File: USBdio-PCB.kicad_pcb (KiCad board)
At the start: 2 copper layers, 201.3 x 72.4 mm, 71 parts, among them P0 TE_RELAY_(ORWH-SH-112D), P1 TE_RELAY_(ORWH-SH-112D), P2 TE_RELAY_(ORWH-SH-112D), P3 TE_RELAY_(ORWH-SH-112D), P4 TE_RELAY_(ORWH-SH-112D), P5 TE_RELAY_(ORWH-SH-112D), P6 TE_RELAY_(ORWH-SH-112D), P7 TE_RELAY_(ORWH-SH-112D), Q1 Q_NPN_EBC, Q10 Q_NPN, Q11 Q_NPN, Q12 Q_NPN, Q13 Q_NPN, Q14 Q_NPN, Q15 Q_NPN, Q16 Q_NPN, Q17 Q_NPN, Q2 Q_NPN_EBC, Q3 Q_NPN_EBC, Q4 Q_NPN_EBC, Q5 Q_NPN_EBC, Q6 Q_NPN_EBC, Q7 Q_NPN_EBC, Q8 Q_NPN_EBC, Q9 Q_NPN_EBC, U1 Arduino_Nano

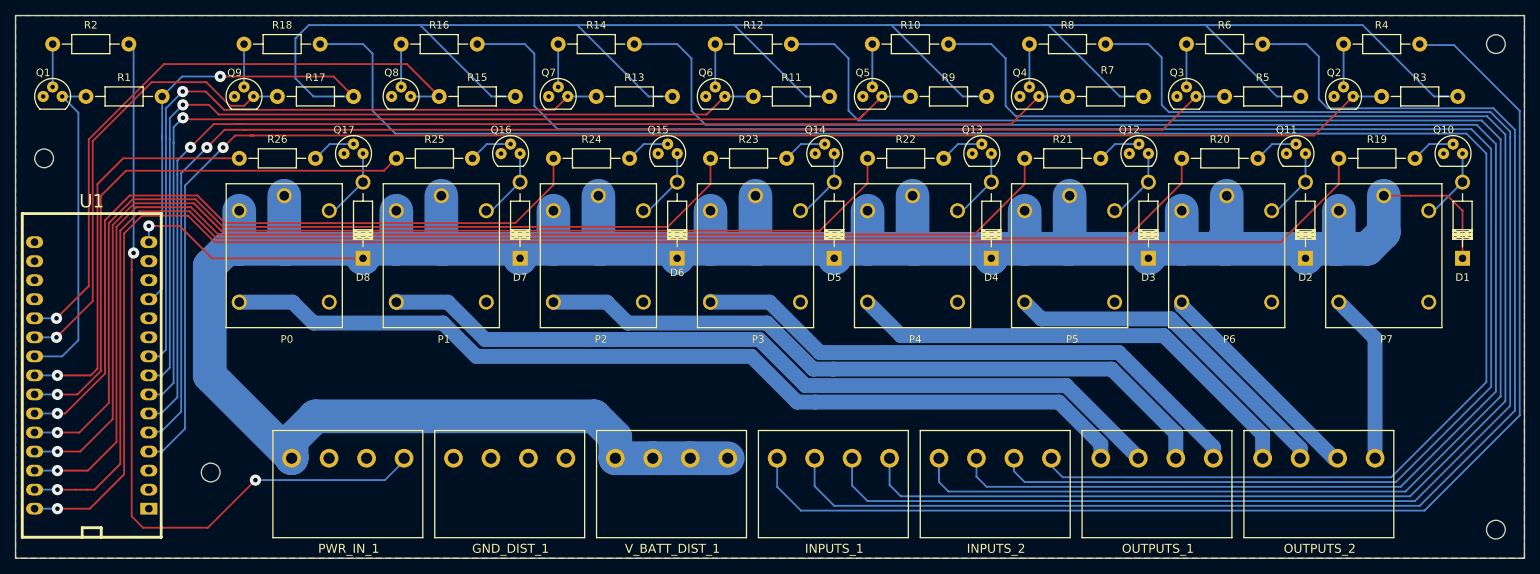
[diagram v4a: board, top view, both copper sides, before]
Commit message: changed default traces from 0.2 mm to 0.4 mm
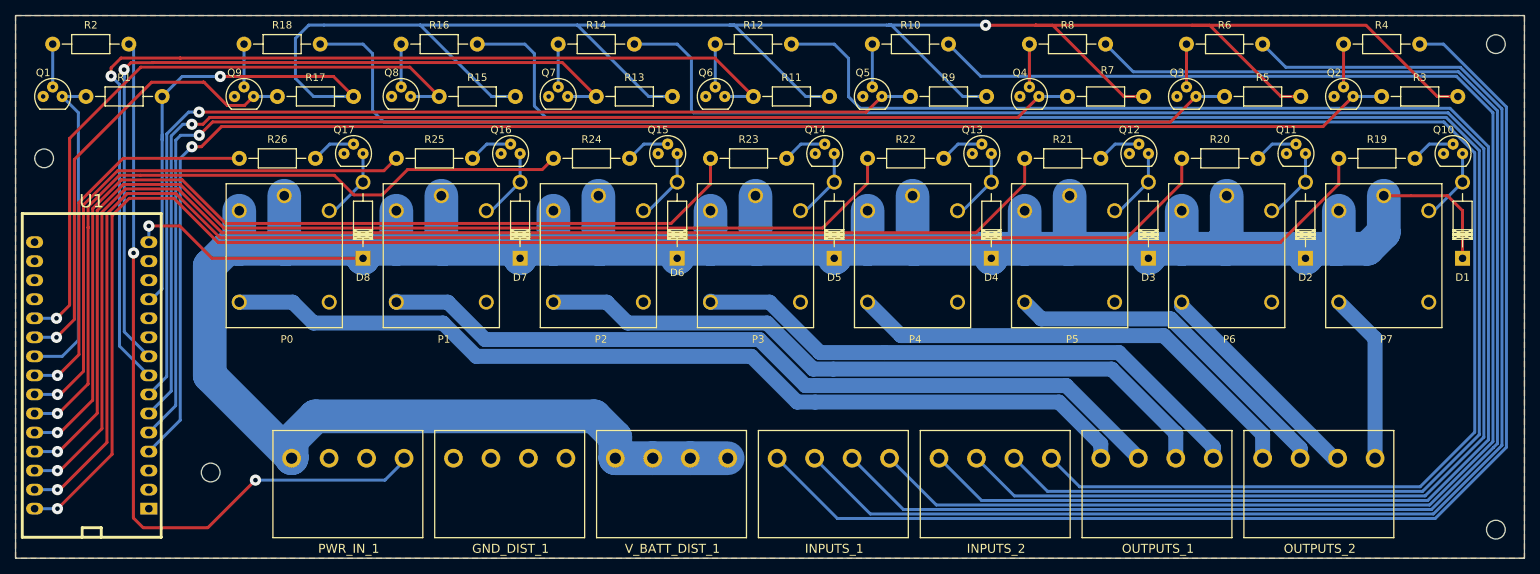
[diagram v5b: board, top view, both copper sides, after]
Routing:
- net Net-(Q6-Pad3): track 116.7 -> 135.3 mm
- net Net-(Q7-Pad3): track 94.9 -> 108.7 mm
- net Net-(INPUTS_1-Pad2): track 182.7 -> 179.0 mm
- net Net-(INPUTS_1-Pad3): track 196.7 -> 192.9 mm
- net Net-(INPUTS_1-Pad4): track 210.2 -> 206.9 mm
- net Net-(R23-Pad2): track 124.4 -> 127.1 mm
- net Net-(R26-Pad2): track 53.7 -> 51.2 mm
- net Net-(R22-Pad2): track 147.5 -> 149.9 mm
- net Net-(INPUTS_2-Pad1): track 222.1 -> 219.8 mm
- net Net-(Q5-Pad3): track 139.2 -> 137.0 mm
- net Net-(Q3-Pad3): track 181.2 -> 183.2 mm
- net Net-(R21-Pad2): track 171.2 -> 173.1 mm
- net Net-(INPUTS_1-Pad1): track 167.1 -> 165.2 mm
- net Net-(R1-Pad2): track 332.8 -> 334.6 mm, vias 1 -> 2
- net Net-(R19-Pad2): track 217.1 -> 218.9 mm
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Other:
- net class Default: trace_width 0.25 -> 0.4

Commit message: removed ground planes
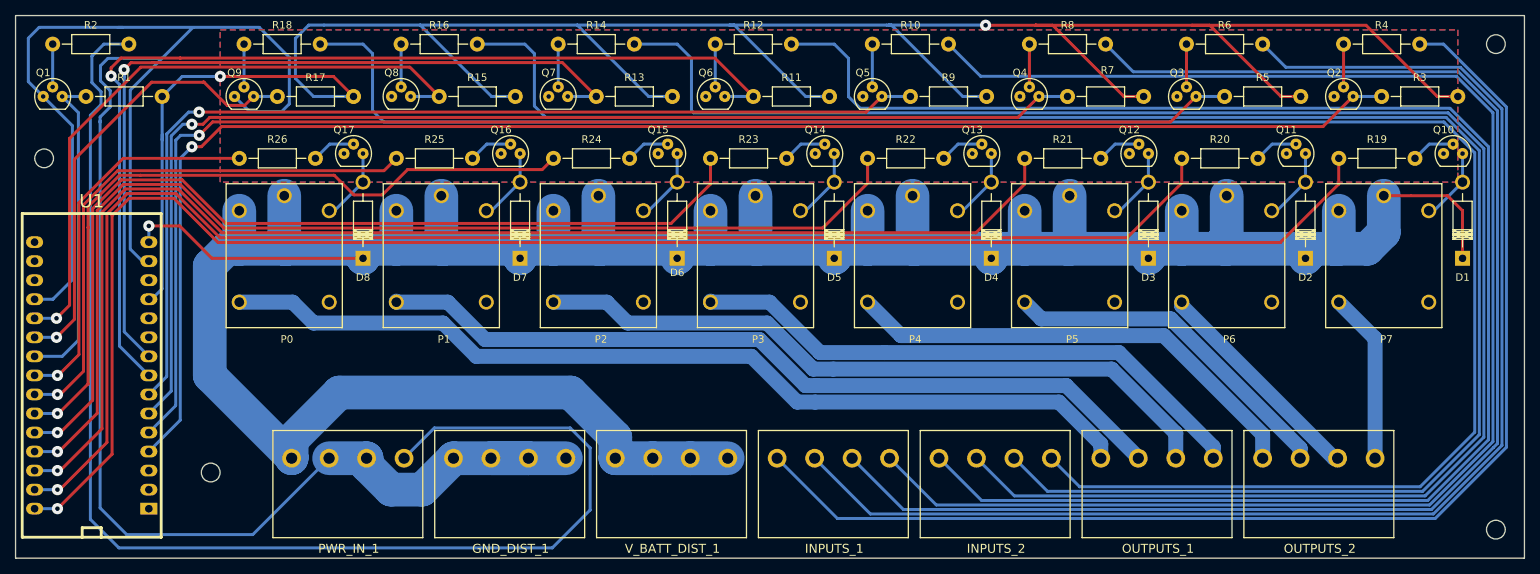
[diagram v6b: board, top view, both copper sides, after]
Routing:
- net GND: track 0.00 -> 275.9 mm
- net Net-(PWR_IN_1-Pad4): track 104.9 -> 175.1 mm, vias 2 -> 0
- net Net-(D1-Pad1): track 427.1 -> 429.7 mm

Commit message: initial commit of deutsch enclosure layout
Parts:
- removed REF** (x4): MountingHole_2.5mm, Mounting_Holes:MountingHole_2.5mm
- removed U1: Arduino_Nano, USBdio-PCB:ARDUINO_NANO
- added CONN_1: DEUTSCH_CONN_(DTM13-12PA-12PB-R008), USBdio-PCB:DEUTSCH_CONN_(DTM13-12PA-12PB-R008), F.Cu at (146.4, 137.7)
- added IC1: ATMEGA328-P, Housings_DIP:DIP-28_W7.62mm_LongPads, F.Cu at (130.1, 68.3)
- D1, D2, D3, D4, D5, D6, D7, D8: footprint Diodes_ThroughHole:Diode_DO-41_SOD81_Horizontal_RM10 -> Resistors_SMD:R_1206_HandSoldering; moved to B.Cu
- Q1, Q2, Q3, Q4, Q5, Q6, Q7, Q8, Q9: value Q_NPN_EBC -> Q_NPN_BEC; footprint USBdio-PCB:TO-92_big_pads -> TO_SOT_Packages_SMD:SOT-23_Handsoldering; moved to B.Cu
- Q10, Q11, Q12, Q13, Q14, Q15, Q16, Q17: footprint USBdio-PCB:TO-92_big_pads -> TO_SOT_Packages_SMD:SOT-23_Handsoldering; moved to B.Cu
- R1, R10, R11, R12, R13, R14, R15, R16, R17, R18, R19, R2, R20, R21, R22, R23, R24, R25, R26, R3, R4, R5, R6, R7, R8, R9: footprint Resistors_ThroughHole:Resistor_Horizontal_RM10mm -> Resistors_SMD:R_1206_HandSoldering; moved to B.Cu
- moved GND_DIST_1 144.6 mm to (105.2, 266.5)
- moved INPUTS_1 144.6 mm to (148.4, 266.5)
- moved INPUTS_2 144.6 mm to (170.0, 266.5)
- moved OUTPUTS_1 144.6 mm to (191.6, 266.5)
- moved OUTPUTS_2 144.6 mm to (213.2, 266.5)
- moved PWR_IN_1 144.6 mm to (83.6, 266.5)
- moved V_BATT_DIST_1 144.6 mm to (126.8, 266.5)
- moved R2 92.9 mm to (143.1, 80.8), turned to 270 degrees
- moved Q1 92.6 mm to (142.6, 74.3), turned to 180 degrees
- moved R1 90.4 mm to (146.1, 74.8), turned to 270 degrees
- moved R3 76.6 mm to (154.6, 53.8), turned to 90 degrees
- moved R4 68.7 mm to (157.6, 47.3), turned to 90 degrees
- moved Q2 67.1 mm to (158.1, 53.8)
- moved D1 65.3 mm to (174.1, 92.3), turned to 0 degrees
- moved R5 64.6 mm to (146.1, 53.8), turned to 90 degrees
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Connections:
- Q1 pad 1: GND -> Net-(Q1-Pad1)
- Q1 pad 2: Net-(Q1-Pad2) -> GND
- Q10 pad 1: GND -> Net-(Q10-Pad1)
- Q10 pad 2: Net-(Q10-Pad2) -> GND
- Q11 pad 1: GND -> Net-(Q11-Pad1)
- Q11 pad 2: Net-(Q11-Pad2) -> GND
- Q12 pad 1: GND -> Net-(Q12-Pad1)
- Q12 pad 2: Net-(Q12-Pad2) -> GND
- Q13 pad 1: GND -> Net-(Q13-Pad1)
- Q13 pad 2: Net-(Q13-Pad2) -> GND
- Q14 pad 1: GND -> Net-(Q14-Pad1)
- Q14 pad 2: Net-(Q14-Pad2) -> GND
- Q15 pad 1: GND -> Net-(Q15-Pad1)
- Q15 pad 2: Net-(Q15-Pad2) -> GND
- Q16 pad 1: GND -> Net-(Q16-Pad1)
- Q16 pad 2: Net-(Q16-Pad2) -> GND
- Q17 pad 1: GND -> Net-(Q17-Pad1)
- Q17 pad 2: Net-(Q17-Pad2) -> GND
- Q2 pad 1: GND -> Net-(Q2-Pad1)
- Q2 pad 2: Net-(Q2-Pad2) -> GND
- Q3 pad 1: GND -> Net-(Q3-Pad1)
- Q3 pad 2: Net-(Q3-Pad2) -> GND
- Q4 pad 1: GND -> Net-(Q4-Pad1)
- Q4 pad 2: Net-(Q4-Pad2) -> GND
- Q5 pad 1: GND -> Net-(Q5-Pad1)
- Q5 pad 2: Net-(Q5-Pad2) -> GND
- Q6 pad 1: GND -> Net-(Q6-Pad1)
- Q6 pad 2: Net-(Q6-Pad2) -> GND
- Q7 pad 1: GND -> Net-(Q7-Pad1)
- Q7 pad 2: Net-(Q7-Pad2) -> GND
- Q8 pad 1: GND -> Net-(Q8-Pad1)
- Q8 pad 2: Net-(Q8-Pad2) -> GND
- Q9 pad 1: GND -> Net-(Q9-Pad1)
- Q9 pad 2: Net-(Q9-Pad2) -> GND
- R10 pad 1: Net-(Q5-Pad2) -> Net-(Q5-Pad1)
- R12 pad 1: Net-(Q6-Pad2) -> Net-(Q6-Pad1)
- R14 pad 1: Net-(Q7-Pad2) -> Net-(Q7-Pad1)
- R16 pad 1: Net-(Q8-Pad2) -> Net-(Q8-Pad1)
- R18 pad 1: Net-(Q9-Pad2) -> Net-(Q9-Pad1)
- R19 pad 1: Net-(Q10-Pad2) -> Net-(Q10-Pad1)
- R2 pad 1: Net-(Q1-Pad2) -> Net-(Q1-Pad1)
- R20 pad 1: Net-(Q11-Pad2) -> Net-(Q11-Pad1)
- R21 pad 1: Net-(Q12-Pad2) -> Net-(Q12-Pad1)
- R22 pad 1: Net-(Q13-Pad2) -> Net-(Q13-Pad1)
- R23 pad 1: Net-(Q14-Pad2) -> Net-(Q14-Pad1)
- R24 pad 1: Net-(Q15-Pad2) -> Net-(Q15-Pad1)
- R25 pad 1: Net-(Q16-Pad2) -> Net-(Q16-Pad1)
- R26 pad 1: Net-(Q17-Pad2) -> Net-(Q17-Pad1)
- R4 pad 1: Net-(Q2-Pad2) -> Net-(Q2-Pad1)
- R6 pad 1: Net-(Q3-Pad2) -> Net-(Q3-Pad1)
- R8 pad 1: Net-(Q4-Pad2) -> Net-(Q4-Pad1)
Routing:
- net Net-(D1-Pad1): track 429.7 -> 0.00 mm, vias 1 -> 0
- net Net-(R1-Pad2): track 334.6 -> 0.00 mm, vias 2 -> 0
- net GND: track 275.9 -> 0.00 mm
- net Net-(INPUTS_2-Pad4): track 262.9 -> 0.00 mm
- net Net-(INPUTS_2-Pad3): track 248.0 -> 0.00 mm
- net Net-(INPUTS_2-Pad2): track 234.8 -> 0.00 mm
- net Net-(INPUTS_2-Pad1): track 219.8 -> 0.00 mm
- net Net-(IC1-Pad18): track 218.9 -> 0.00 mm, vias 1 -> 0
- net Net-(INPUTS_1-Pad4): track 206.9 -> 0.00 mm
- net Net-(IC1-Pad23): track 204.5 -> 0.00 mm, vias 1 -> 0
- net Net-(IC1-Pad17): track 195.7 -> 0.00 mm, vias 1 -> 0
- net Net-(INPUTS_1-Pad3): track 192.9 -> 0.00 mm
- net Net-(IC1-Pad24): track 183.2 -> 0.00 mm, vias 1 -> 0
- net Net-(INPUTS_1-Pad2): track 179.0 -> 0.00 mm
- net Net-(PWR_IN_1-Pad4): track 175.1 -> 0.00 mm
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- removed copper zone on B.Cu, net GND
- removed copper zone on F.Cu, net GND
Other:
- board size 201.3 x 72.4 mm -> 82.5 x 101.6 mm

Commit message: all footprints added.  ready for traces.
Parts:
- removed GND_DIST_1, INPUTS_1, INPUTS_2, OUTPUTS_1, OUTPUTS_2, PWR_IN_1, V_BATT_DIST_1: CONN_01X04, USBdio-PCB:PHX_HDR_4_POS_(1933202)
- added D9: D_Schottky, USBdio-PCB:SCHOTTKY_(PMEG3030EP,115), B.Cu at (177.6, 65.8)
- added P8: CONN_01X03, Pin_Headers:Pin_Header_Straight_1x03, F.Cu at (159.1, 134.8)
- added R27: 1M, Resistors_SMD:R_1206_HandSoldering, B.Cu at (153.6, 77.3)
- added R28: 10k, Resistors_SMD:R_1206_HandSoldering, B.Cu at (119.1, 68.3)
- added U1: NCV7805BDTRKG, USBdio-PCB:REGULATOR_(NCV7805BDTRKG), B.Cu at (175.1, 56.8)
- added X1: CRYSTAL_SMD, USBdio-PCB:RESONATOR_(CSTCE16M0V53C-R0), B.Cu at (152.1, 72.8)
- P0, P1, P2, P3, P4, P5, P6, P7: value TE_RELAY_(ORWH-SH-112D) -> RELAY_(JSM1A-12V-4); footprint USBdio-PCB:TE_RELAY_(ORWH-SH-112D) -> USBdio-PCB:RELAY_(JSM1A-12V-4)
- R19, R20, R21, R22, R23, R24, R25, R26: value 1k -> 680
- moved P0 2.70 mm to (116.4, 112.0)
- moved P1 2.70 mm to (132.4, 112.0)
- moved P2 2.70 mm to (148.4, 112.0)
- moved P3 2.70 mm to (164.4, 112.0)
- moved D5 2.50 mm to (174.1, 114.8)
- moved D6 2.50 mm to (158.1, 114.8)
- moved D7 2.50 mm to (142.1, 114.8)
- moved D8 2.50 mm to (126.1, 114.8)
- moved Q14 2.50 mm to (176.1, 119.3)
- moved Q15 2.50 mm to (160.1, 119.3)
- moved Q16 2.50 mm to (144.1, 119.3)
- moved Q17 2.50 mm to (128.1, 119.3)
- moved R23 2.50 mm to (180.1, 118.8)
- moved R24 2.50 mm to (164.1, 118.8)
- moved R25 2.50 mm to (148.1, 118.8)
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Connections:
- CONN_1 pad A10: Net-(CONN_1-PadA10) -> RLY1
- CONN_1 pad A11: Net-(CONN_1-PadA11) -> RLY2
- CONN_1 pad A12: Net-(CONN_1-PadA12) -> RLY3
- CONN_1 pad A2: Net-(CONN_1-PadA2) -> GND
- CONN_1 pad A3: Net-(CONN_1-PadA3) -> GND
- CONN_1 pad A9: Net-(CONN_1-PadA9) -> RLY0
- CONN_1 pad B1: Net-(CONN_1-PadB1) -> Net-(CONN_1-PadA1)
- CONN_1 pad B10: Net-(CONN_1-PadB10) -> RLY5
- CONN_1 pad B11: Net-(CONN_1-PadB11) -> RLY6
- CONN_1 pad B12: Net-(CONN_1-PadB12) -> RLY7
- CONN_1 pad B2: Net-(CONN_1-PadB2) -> Net-(CONN_1-PadA1)
- CONN_1 pad B3: Net-(CONN_1-PadB3) -> GND
- CONN_1 pad B4: Net-(CONN_1-PadB4) -> GND
- CONN_1 pad B9: Net-(CONN_1-PadB9) -> RLY4
- IC1 pad 20: Net-(IC1-Pad20) -> +5V
- IC1 pad 7: Net-(IC1-Pad7) -> +5V
- P0 pad 1: Net-(D1-Pad1) -> Net-(CONN_1-PadA1)
- P0 pad 2: Net-(D8-Pad2) -> Net-(D1-Pad1)
- P0 pad 3: Net-(D1-Pad1) -> RLY0
- P0 pad 5: Net-(P0-Pad5) -> Net-(D8-Pad2)
- P1 pad 1: Net-(D1-Pad1) -> Net-(CONN_1-PadA1)
- P1 pad 2: Net-(D7-Pad2) -> Net-(D1-Pad1)
- P1 pad 3: Net-(D1-Pad1) -> RLY1
- P1 pad 5: Net-(P1-Pad5) -> Net-(D7-Pad2)
- P2 pad 1: Net-(D1-Pad1) -> Net-(CONN_1-PadA1)
- P2 pad 2: Net-(D6-Pad2) -> Net-(D1-Pad1)
- P2 pad 3: Net-(D1-Pad1) -> RLY2
- P2 pad 5: Net-(P2-Pad5) -> Net-(D6-Pad2)
- P3 pad 1: Net-(D1-Pad1) -> Net-(CONN_1-PadA1)
- P3 pad 2: Net-(D5-Pad2) -> Net-(D1-Pad1)
- P3 pad 3: Net-(D1-Pad1) -> RLY3
- P3 pad 5: Net-(P3-Pad5) -> Net-(D5-Pad2)
- P4 pad 1: Net-(D1-Pad1) -> Net-(CONN_1-PadA1)
- P4 pad 2: Net-(D4-Pad2) -> Net-(D1-Pad1)
- P4 pad 3: Net-(D1-Pad1) -> RLY4
- P4 pad 5: Net-(P4-Pad5) -> Net-(D4-Pad2)
- P5 pad 1: Net-(D1-Pad1) -> Net-(CONN_1-PadA1)
- P5 pad 2: Net-(D3-Pad2) -> Net-(D1-Pad1)
- P5 pad 3: Net-(D1-Pad1) -> RLY5
- P5 pad 5: Net-(P5-Pad5) -> Net-(D3-Pad2)
- P6 pad 1: Net-(D1-Pad1) -> Net-(CONN_1-PadA1)
- P6 pad 2: Net-(D2-Pad2) -> Net-(D1-Pad1)
- P6 pad 3: Net-(D1-Pad1) -> RLY6
- P6 pad 5: Net-(P6-Pad5) -> Net-(D2-Pad2)
- P7 pad 1: Net-(D1-Pad1) -> Net-(CONN_1-PadA1)
- P7 pad 2: Net-(D1-Pad2) -> Net-(D1-Pad1)
- P7 pad 3: Net-(D1-Pad1) -> RLY7
- P7 pad 5: Net-(P7-Pad5) -> Net-(D1-Pad2)
- R1 pad 2: Net-(R1-Pad2) -> +5V
- R10 pad 2: Net-(INPUTS_1-Pad4) -> Net-(CONN_1-PadA8)
- R11 pad 2: Net-(R1-Pad2) -> +5V
- R12 pad 2: Net-(INPUTS_2-Pad1) -> Net-(CONN_1-PadB5)
- R13 pad 2: Net-(R1-Pad2) -> +5V
- R14 pad 2: Net-(INPUTS_2-Pad2) -> Net-(CONN_1-PadB6)
- R15 pad 2: Net-(R1-Pad2) -> +5V
- R16 pad 2: Net-(INPUTS_2-Pad3) -> Net-(CONN_1-PadB7)
- R17 pad 2: Net-(R1-Pad2) -> +5V
- R18 pad 2: Net-(INPUTS_2-Pad4) -> Net-(CONN_1-PadB8)
- R2 pad 2: Net-(PWR_IN_1-Pad4) -> Net-(CONN_1-PadA4)
- R3 pad 2: Net-(R1-Pad2) -> +5V
- R4 pad 2: Net-(INPUTS_1-Pad1) -> Net-(CONN_1-PadA5)
- R5 pad 2: Net-(R1-Pad2) -> +5V
- R6 pad 2: Net-(INPUTS_1-Pad2) -> Net-(CONN_1-PadA6)
- R7 pad 2: Net-(R1-Pad2) -> +5V
- R8 pad 2: Net-(INPUTS_1-Pad3) -> Net-(CONN_1-PadA7)
- R9 pad 2: Net-(R1-Pad2) -> +5V
